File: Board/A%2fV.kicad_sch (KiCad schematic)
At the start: 25 parts, among them IC2 74245DW, IC6 74138D, X2 D-SUB15-HDR15RA

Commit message: Ultipet 1.0A final
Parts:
- removed IC6: 74138D, cbm_ultipet_v1:SO16, symbol cbm_ultipet_v1-eagle-import:74138D
- removed R21: 2k, cbm_ultipet_v1:0204V, symbol cbm_ultipet_v1-eagle-import:R-EU_0204/2V
- removed R3: 10k, cbm_ultipet_v1:0204V, symbol cbm_ultipet_v1-eagle-import:R-EU_0204/2V
- added D9: 1N4148DO35-7, cbm_ultipet_v1:DO35-7, symbol cbm_ultipet_v1-eagle-import:1N4148DO35-7
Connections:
- net at IC2.11 (B8): now also D9.A
- net at IC2.12 (B7): now also D1.A
- net IGOUT: now reaches IC2.8 (A7)
- net IGOUT: no longer IC2.9 (A8)
- net at D7.C, R18.1: no longer R19.1, R20.1
- net at D1.C: now also R19.1
- net at R14.2, R19.2, U$10.2 (1)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: no longer D1.A
- net IOUT renamed IBOUT
- new net: D9.C, R20.1
- new net IROUT: IC2.9 (A8)
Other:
- note added: "CSA-ULTIPET-V1.0A-20240331"
- note removed: ""Brown Fix" Changes dark yellow into Brown Used to be included in monitors"
- note removed: "CSA-ULTRACPU-V1.1A-20220820"

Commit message: ultipet 1.1a board
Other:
- note added: "CBM-ULTIPET-V1.1A"
- note removed: "CBM-ULTIPET-V1.0A"
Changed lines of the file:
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@@
 		)
 	)
-	(text "CBM-ULTIPET-V1.0A"
+	(text "CBM-ULTIPET-V1.1A"
 		(exclude_from_sim no)
 		(at 208.28 144.78 0)

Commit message: clamp diodes for joysticks
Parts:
- D1, D2, D3, D4, D7, D9: footprint cbm_ultipet_v1:DO35-7 -> Diode_THT:D_DO-35_SOD27_P7.62mm_Horizontal
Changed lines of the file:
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@@
 			)
 		)
-		(property "Footprint" "cbm_ultipet_v1:DO35-7"
+		(property "Footprint" "Diode_THT:D_DO-35_SOD27_P7.62mm_Horizontal"
 			(at 139.7 93.98 0)
 			(effects
@@
 			)
 		)
-		(property "Footprint" "cbm_ultipet_v1:DO35-7"
+		(property "Footprint" "Diode_THT:D_DO-35_SOD27_P7.62mm_Horizontal"
 			(at 139.7 78.74 0)
 			(effects
@@
 			)
 		)
-		(property "Footprint" "cbm_ultipet_v1:DO35-7"
+		(property "Footprint" "Diode_THT:D_DO-35_SOD27_P7.62mm_Horizontal"
 			(at 139.7 116.84 0)
 			(effects
@@
 			)
 		)
-		(property "Footprint" "cbm_ultipet_v1:DO35-7"
+		(property "Footprint" "Diode_THT:D_DO-35_SOD27_P7.62mm_Horizontal"
 			(at 139.7 86.36 0)
 			(effects
@@
 			)
 		)
-		(property "Footprint" "cbm_ultipet_v1:DO35-7"
+		(property "Footprint" "Diode_THT:D_DO-35_SOD27_P7.62mm_Horizontal"
 			(at 139.7 101.6 0)
 			(effects
@@
 			)
 		)
-		(property "Footprint" "cbm_ultipet_v1:DO35-7"
+		(property "Footprint" "Diode_THT:D_DO-35_SOD27_P7.62mm_Horizontal"
 			(at 139.7 109.22 0)
 			(effects

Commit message: more layout work
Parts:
- removed D1, D2, D3, D4, D7, D9: 1N4148DO35-7, Diode_THT:D_DO-35_SOD27_P7.62mm_Horizontal, symbol cbm_ultipet_v1-eagle-import:1N4148DO35-7
- added D1, D2, D3, D36, D4, D7: 1N4448, Diode_THT:D_DO-35_SOD27_P7.62mm_Horizontal, symbol Diode:1N4448
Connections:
- net BLUE: now also D2.2 (A)
- net GREEN: now also D1.2 (A)
- net INTENSITY: now also D3.2 (A)
- net RED: now also D36.2 (A)
- net at R15.1: now also D36.1 (K)
- net at IC2.11 (B8): now also D7.2 (A)
- net at IC2.12 (B7): now also D4.2 (A)
- net at R13.1: now also D2.1 (K)
- net at R20.1: now also D7.1 (K)
- net at R14.1: now also D1.1 (K)
- net at R18.1: now also D3.1 (K)
- net at R19.1: now also D4.1 (K)

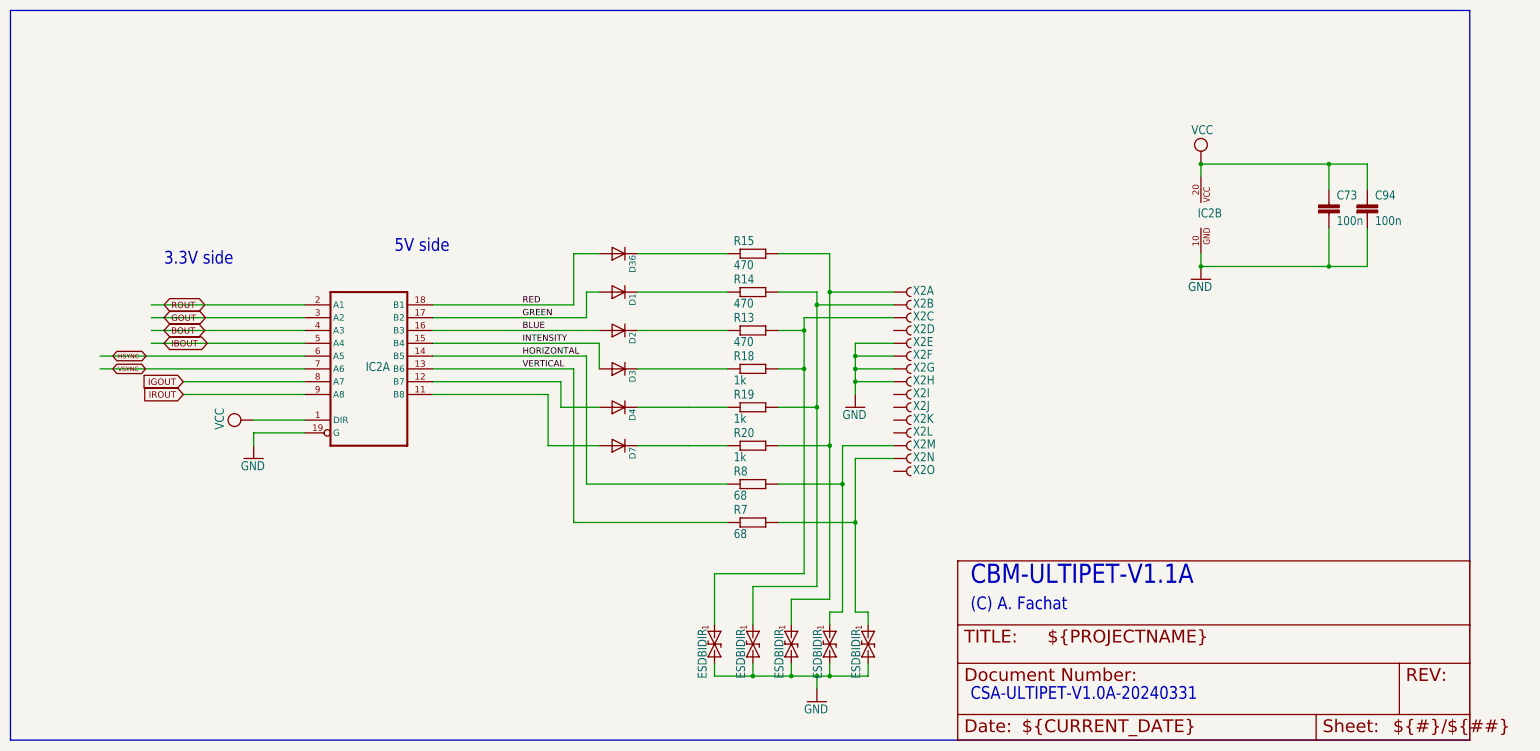
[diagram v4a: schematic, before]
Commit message: generic add digital video out connector
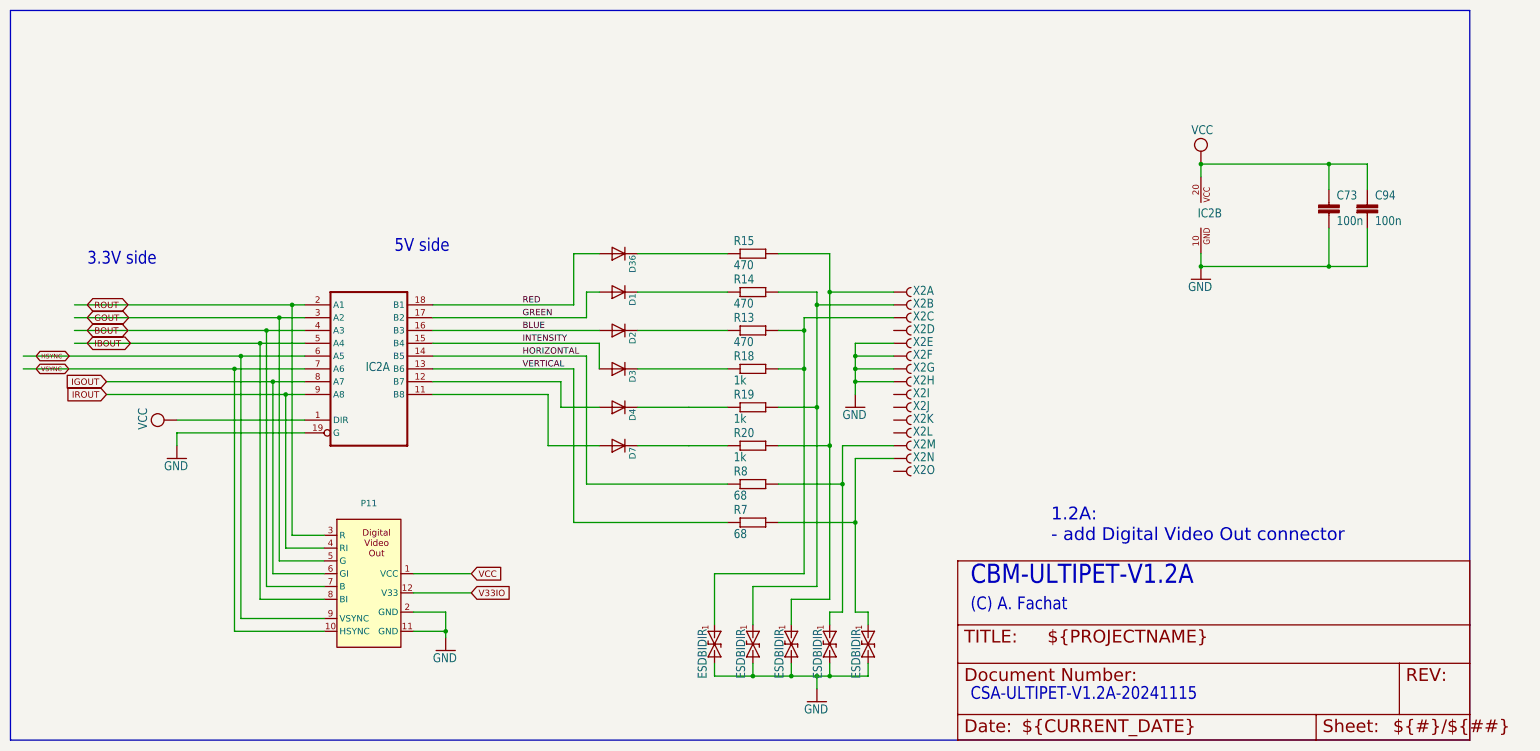
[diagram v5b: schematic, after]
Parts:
- added P11: ~, Connector_PinHeader_2.54mm:PinHeader_2x06_P2.54mm_Vertical, symbol cbm_ultipet_v1-eagle-import:DVO-Connector
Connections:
- net BOUT: now also P11.7 (B)
- net GND: now also P11.11 (GND), P11.2 (GND)
- net GOUT: now also P11.5 (G)
- net HSYNC: now also P11.9 (VSYNC)
- net IBOUT: now also P11.8 (BI)
- net IGOUT: now also P11.6 (GI)
- net IROUT: now also P11.4 (RI)
- net ROUT: now also P11.3 (R)
- net VCC: now also P11.1 (VCC)
- net VSYNC: now also P11.10 (HSYNC)
- new net V33IO: P11.12 (V33)
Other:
- note added: "1.2A: - add Digital Video Out connector"
- note added: "CBM-ULTIPET-V1.2A"
- note added: "CSA-ULTIPET-V1.2A-20241115"
- note removed: "CBM-ULTIPET-V1.1A"
- note removed: "CSA-ULTIPET-V1.0A-20240331"

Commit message: work on 1.3
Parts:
- IC2: footprint cbm_ultipet_v1:SO20W@1 -> Package_SO:SOP-20_7.5x12.8mm_P1.27mm

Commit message: work on r1.3
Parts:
- X2: footprint cbm_ultipet_v1:HDR15RA -> Connector_Dsub:DSUB-15-HD_Socket_Horizontal_P2.29x2.54mm_EdgePinOffset8.35mm_Housed_MountingHolesOffset10.89mm
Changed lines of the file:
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@@
 			)
 		)
-		(property "Footprint" "cbm_ultipet_v1:HDR15RA"
+		(property "Footprint" "Connector_Dsub:DSUB-15-HD_Socket_Horizontal_P2.29x2.54mm_EdgePinOffset8.35mm_Housed_MountingHolesOffset10.89mm"
 			(at 195.58 91.44 0)
 			(effects
@@
 			)
 		)
-		(property "Footprint" "cbm_ultipet_v1:HDR15RA"
+		(property "Footprint" "Connector_Dsub:DSUB-15-HD_Socket_Horizontal_P2.29x2.54mm_EdgePinOffset8.35mm_Housed_MountingHolesOffset10.89mm"
 			(at 195.58 121.92 0)
 			(effects
@@
 			)
 		)
-		(property "Footprint" "cbm_ultipet_v1:HDR15RA"
+		(property "Footprint" "Connector_Dsub:DSUB-15-HD_Socket_Horizontal_P2.29x2.54mm_EdgePinOffset8.35mm_Housed_MountingHolesOffset10.89mm"
 			(at 195.58 86.36 0)
 			(effects
@@
 			)
 		)
-		(property "Footprint" "cbm_ultipet_v1:HDR15RA"
+		(property "Footprint" "Connector_Dsub:DSUB-15-HD_Socket_Horizontal_P2.29x2.54mm_EdgePinOffset8.35mm_Housed_MountingHolesOffset10.89mm"
 			(at 195.58 114.3 0)
 			(effects
@@
 			)
 		)
-		(property "Footprint" "cbm_ultipet_v1:HDR15RA"
+		(property "Footprint" "Connector_Dsub:DSUB-15-HD_Socket_Horizontal_P2.29x2.54mm_EdgePinOffset8.35mm_Housed_MountingHolesOffset10.89mm"
 			(at 195.58 116.84 0)
 			(effects
@@
 			)
 		)
-		(property "Footprint" "cbm_ultipet_v1:HDR15RA"
+		(property "Footprint" "Connector_Dsub:DSUB-15-HD_Socket_Horizontal_P2.29x2.54mm_EdgePinOffset8.35mm_Housed_MountingHolesOffset10.89mm"
 			(at 195.58 104.14 0)
 			(effects
@@
 			)
 		)
-		(property "Footprint" "cbm_ultipet_v1:HDR15RA"
+		(property "Footprint" "Connector_Dsub:DSUB-15-HD_Socket_Horizontal_P2.29x2.54mm_EdgePinOffset8.35mm_Housed_MountingHolesOffset10.89mm"
 			(at 195.58 96.52 0)
 			(effects
@@
 			)
 		)
-		(property "Footprint" "cbm_ultipet_v1:HDR15RA"
+		(property "Footprint" "Connector_Dsub:DSUB-15-HD_Socket_Horizontal_P2.29x2.54mm_EdgePinOffset8.35mm_Housed_MountingHolesOffset10.89mm"
 			(at 195.58 99.06 0)
 			(effects
@@
 			)
 		)
-		(property "Footprint" "cbm_ultipet_v1:HDR15RA"
+		(property "Footprint" "Connector_Dsub:DSUB-15-HD_Socket_Horizontal_P2.29x2.54mm_EdgePinOffset8.35mm_Housed_MountingHolesOffset10.89mm"
 			(at 195.58 109.22 0)
 			(effects
@@
 			)
 		)
-		(property "Footprint" "cbm_ultipet_v1:HDR15RA"
+		(property "Footprint" "Connector_Dsub:DSUB-15-HD_Socket_Horizontal_P2.29x2.54mm_EdgePinOffset8.35mm_Housed_MountingHolesOffset10.89mm"
 			(at 195.58 111.76 0)
 			(effects
@@
 			)
 		)
-		(property "Footprint" "cbm_ultipet_v1:HDR15RA"
+		(property "Footprint" "Connector_Dsub:DSUB-15-HD_Socket_Horizontal_P2.29x2.54mm_EdgePinOffset8.35mm_Housed_MountingHolesOffset10.89mm"
 			(at 195.58 93.98 0)
 			(effects
@@
 			)
 		)
-		(property "Footprint" "cbm_ultipet_v1:HDR15RA"
+		(property "Footprint" "Connector_Dsub:DSUB-15-HD_Socket_Horizontal_P2.29x2.54mm_EdgePinOffset8.35mm_Housed_MountingHolesOffset10.89mm"
 			(at 195.58 106.68 0)
 			(effects
@@
 			)
 		)
-		(property "Footprint" "cbm_ultipet_v1:HDR15RA"
+		(property "Footprint" "Connector_Dsub:DSUB-15-HD_Socket_Horizontal_P2.29x2.54mm_EdgePinOffset8.35mm_Housed_MountingHolesOffset10.89mm"
 			(at 195.58 119.38 0)
 			(effects
@@
 			)
 		)
-		(property "Footprint" "cbm_ultipet_v1:HDR15RA"
+		(property "Footprint" "Connector_Dsub:DSUB-15-HD_Socket_Horizontal_P2.29x2.54mm_EdgePinOffset8.35mm_Housed_MountingHolesOffset10.89mm"
 			(at 195.58 88.9 0)
 			(effects
@@
 			)
 		)
-		(property "Footprint" "cbm_ultipet_v1:HDR15RA"
+		(property "Footprint" "Connector_Dsub:DSUB-15-HD_Socket_Horizontal_P2.29x2.54mm_EdgePinOffset8.35mm_Housed_MountingHolesOffset10.89mm"
 			(at 195.58 101.6 0)
 			(effects
